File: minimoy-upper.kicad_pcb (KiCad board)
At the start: 2 copper layers, 35 x 35 mm, 29 parts, among them J2 Conn_02x02_Odd_Even, J5 AudioJack3_Ground, J6 Conn_02x02_Odd_Even, J7 AudioJack3_Ground, U1 MAX5440EAG, U3 OPA2134, U4 L7805

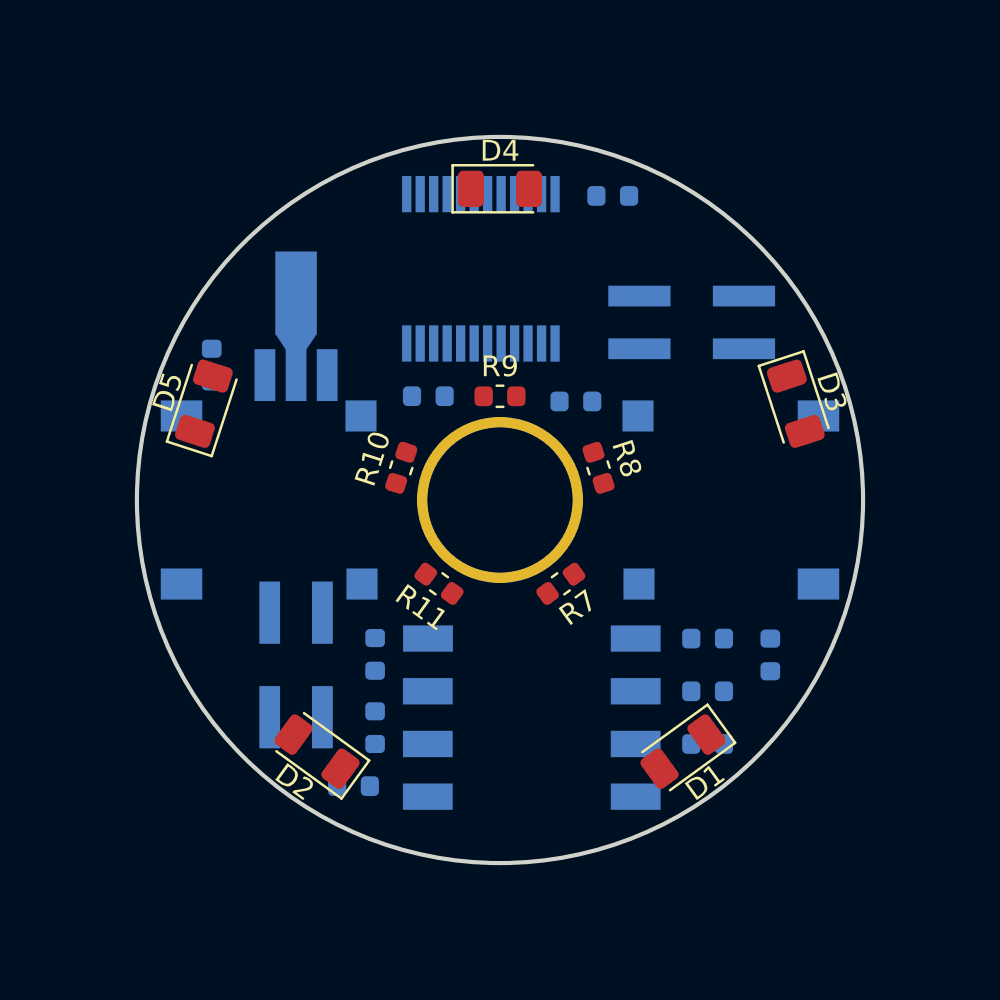
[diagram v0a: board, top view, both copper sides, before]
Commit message: Move 7805 to lower board. Make room for cap on upper board.
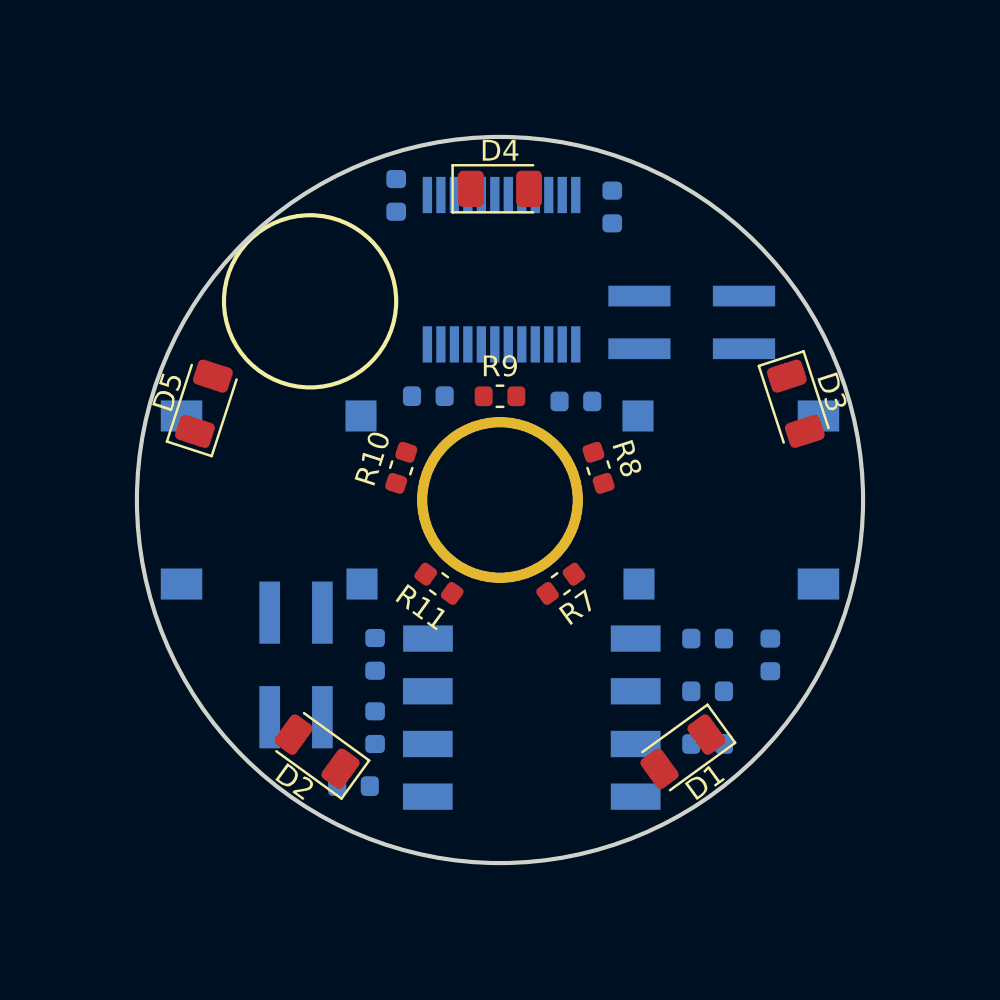
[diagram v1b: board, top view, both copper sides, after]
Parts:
- removed U4: L7805, Package_TO_SOT_SMD:SOT-89-3_Handsoldering
- moved C3 12.1 mm to (95.0, 85.3)
- moved U1 1.00 mm to (100.1, 88.9)
- moved C1 0.53 mm to (105.4, 85.9), turned to 270 degrees
- turned J6 to 270 degrees
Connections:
- J6 pad 2: /VGND_UPPER -> /+5V_UPPER
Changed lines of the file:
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@@
   (general
     (thickness 1.6)
-    (drawings 1)
+    (drawings 2)
     (tracks 0)
     (zones 0)
-    (modules 29)
+    (modules 28)
     (nets 35)
   )
@@
   )
   (module Capacitor_SMD:C_0603_1608Metric (layer B.Cu)
-    (at 105.4355 85.344 180)
+    (at 105.41 85.8775 270)
     (descr "Capacitor SMD 0603 (1608 Metric), square (rectangular) end terminal, IPC_7351 nominal, (Body size source: http://www.tortai-tech.com/upload/download/2011102023233369053.pdf), generated with kicad-footprint-generator")
     (tags capacitor)
     (attr smd)
-    (fp_text reference C1 (at 0 1.43 180) (layer B.SilkS)
-      (effects (font (size 1 1) (thickness 0.15)) (justify mirror))
-    )
-    (fp_text value 0.1uF (at 0 -1.43 180) (layer B.Fab)
+    (fp_text reference C1 (at 0 1.43 270) (layer B.SilkS)
+      (effects (font (size 1 1) (thickness 0.15)) (justify mirror))
+    )
+    (fp_text value 0.1uF (at 0 -1.43 270) (layer B.Fab)
       (effects (font (size 1 1) (thickness 0.15)) (justify mirror))
     )
@@
     (fp_line (start 1.48 0.73) (end 1.48 -0.73) (layer B.CrtYd) (width 0.05))
     (fp_line (start 1.48 -0.73) (end -1.48 -0.73) (layer B.CrtYd) (width 0.05))
-    (fp_text user %R (at 0 0 180) (layer B.Fab)
+    (fp_text user %R (at 0 0 270) (layer B.Fab)
       (effects (font (size 0.4 0.4) (thickness 0.06)) (justify mirror))
     )
-    (pad 1 smd roundrect (at -0.7875 0 180) (size 0.875 0.95) (layers B.Cu B.Paste B.Mask) (roundrect_rratio 0.25)
+    (pad 1 smd roundrect (at -0.7875 0 270) (size 0.875 0.95) (layers B.Cu B.Paste B.Mask) (roundrect_rratio 0.25)
       (net 1 "Net-(C1-Pad1)"))
-    (pad 2 smd roundrect (at 0.7875 0 180) (size 0.875 0.95) (layers B.Cu B.Paste B.Mask) (roundrect_rratio 0.25)
+    (pad 2 smd roundrect (at 0.7875 0 270) (size 0.875 0.95) (layers B.Cu B.Paste B.Mask) (roundrect_rratio 0.25)
       (net 2 /VGND_UPPER))
     (model ${KISYS3DMOD}/Capacitor_SMD.3dshapes/C_0603_1608Metric.wrl
@@
   )
   (module Capacitor_SMD:C_0603_1608Metric (layer B.Cu)
-    (at 86.106 93.4975 270)
+    (at 94.996 85.3185 270)
     (descr "Capacitor SMD 0603 (1608 Metric), square (rectangular) end terminal, IPC_7351 nominal, (Body size source: http://www.tortai-tech.com/upload/download/2011102023233369053.pdf), generated with kicad-footprint-generator")
     (tags capacitor)
@@
   )
   (module Connector_PinSocket_2.54mm:PinSocket_2x02_P2.54mm_Vertical_SMD (layer B.Cu)
-    (at 90.17 107.95 90)
+    (at 90.17 107.95 270)
     (descr "surface-mounted straight socket strip, 2x02, 2.54mm pitch, double cols (from Kicad 4.0.7), script generated")
     (tags "Surface mounted socket strip SMD 2x02 2.54mm double row")
     (attr smd)
-    (fp_text reference J6 (at 0 4.04 90) (layer B.SilkS)
-      (effects (font (size 1 1) (thickness 0.15)) (justify mirror))
-    )
-    (fp_text value Conn_02x02_Odd_Even (at 0 -4.04 90) (layer B.Fab)
-      (effects (font (size 1 1) (thickness 0.15)) (justify mirror))
-    )
-    (fp_text user %R (at 0 0) (layer B.Fab)
+    (fp_text reference J6 (at 0 4.04 270) (layer B.SilkS)
+      (effects (font (size 1 1) (thickness 0.15)) (justify mirror))
+    )
+    (fp_text value Conn_02x02_Odd_Even (at 0 -4.04 270) (layer B.Fab)
+      (effects (font (size 1 1) (thickness 0.15)) (justify mirror))
+    )
+    (fp_text user %R (at 0 0 180) (layer B.Fab)
       (effects (font (size 1 1) (thickness 0.15)) (justify mirror))
     )
@@
     (fp_line (start 2.6 2.6) (end 2.6 2.03) (layer B.SilkS) (width 0.12))
     (fp_line (start -2.6 2.6) (end 2.6 2.6) (layer B.SilkS) (width 0.12))
-    (pad 4 smd rect (at -2.52 -1.27 90) (size 3 1) (layers B.Cu B.Paste B.Mask)
-      (net 2 /VGND_UPPER))
-    (pad 3 smd rect (at 2.52 -1.27 90) (size 3 1) (layers B.Cu B.Paste B.Mask)
+    (pad 4 smd rect (at -2.52 -1.27 270) (size 3 1) (layers B.Cu B.Paste B.Mask)
+      (net 2 /VGND_UPPER))
+    (pad 3 smd rect (at 2.52 -1.27 270) (size 3 1) (layers B.Cu B.Paste B.Mask)
       (net 24 /-12V_UPPER))
-    (pad 2 smd rect (at -2.52 1.27 90) (size 3 1) (layers B.Cu B.Paste B.Mask)
-      (net 2 /VGND_UPPER))
-    (pad 1 smd rect (at 2.52 1.27 90) (size 3 1) (layers B.Cu B.Paste B.Mask)
+    (pad 2 smd rect (at -2.52 1.27 270) (size 3 1) (layers B.Cu B.Paste B.Mask)
+      (net 4 /+5V_UPPER))
+    (pad 1 smd rect (at 2.52 1.27 270) (size 3 1) (layers B.Cu B.Paste B.Mask)
       (net 25 /+12V_UPPER))
     (model ${KISYS3DMOD}/Connector_PinSocket_2.54mm.3dshapes/PinSocket_2x02_P2.54mm_Vertical_SMD.wrl
@@
   )
   (module Package_SO:SSOP-24_5.3x8.2mm_P0.65mm (layer B.Cu)
-    (at 99.079 88.856 270)
+    (at 100.076 88.9 270)
     (descr "24-Lead Plastic Shrink Small Outline (SS)-5.30 mm Body [SSOP] (see Microchip Packaging Specification 00000049BS.pdf)")
     (tags "SSOP 0.65")
@@
       (net 24 /-12V_UPPER))
   )
-  (module Package_TO_SOT_SMD:SOT-89-3_Handsoldering (layer B.Cu)
-    (at 90.17 92 90)
-    (descr "SOT-89-3 Handsoldering")
-    (tags "SOT-89-3 Handsoldering")
-    (attr smd)
-    (fp_text reference U4 (at 0.45 3.3 90) (layer B.SilkS)
-      (effects (font (size 1 1) (thickness 0.15)) (justify mirror))
-    )
-    (fp_text value L7805 (at 0.5 -3.15 90) (layer B.Fab)
-      (effects (font (size 1 1) (thickness 0.15)) (justify mirror))
-    )
-    (fp_text user %R (at 0.38 0) (layer B.Fab)
-      (effects (font (size 0.6 0.6) (thickness 0.09)) (justify mirror))
-    )
-    (fp_line (start -3.5 -2.55) (end 4.25 -2.55) (layer B.CrtYd) (width 0.05))
-    (fp_line (start 4.25 -2.55) (end 4.25 2.55) (layer B.CrtYd) (width 0.05))
-    (fp_line (start 4.25 2.55) (end -3.5 2.55) (layer B.CrtYd) (width 0.05))
-    (fp_line (start -3.5 2.55) (end -3.5 -2.55) (layer B.CrtYd) (width 0.05))
-    (fp_line (start 1.78 -1.2) (end 1.78 -2.4) (layer B.SilkS) (width 0.12))
-    (fp_line (start 1.78 -2.4) (end -0.92 -2.4) (layer B.SilkS) (width 0.12))
-    (fp_line (start -2.22 2.4) (end 1.78 2.4) (layer B.SilkS) (width 0.12))
-    (fp_line (start 1.78 2.4) (end 1.78 1.2) (layer B.SilkS) (width 0.12))
-    (fp_line (start -0.92 1.51) (end -0.13 2.3) (layer B.Fab) (width 0.1))
-    (fp_line (start 1.68 2.3) (end 1.68 -2.3) (layer B.Fab) (width 0.1))
-    (fp_line (start 1.68 -2.3) (end -0.92 -2.3) (layer B.Fab) (width 0.1))
-    (fp_line (start -0.92 -2.3) (end -0.92 1.51) (layer B.Fab) (width 0.1))
-    (fp_line (start -0.13 2.3) (end 1.68 2.3) (layer B.Fab) (width 0.1))
-    (pad 1 smd rect (at -1.98 1.5 180) (size 1 2.5) (layers B.Cu B.Paste B.Mask)
-      (net 25 /+12V_UPPER))
-    (pad 2 smd rect (at -1.98 0 180) (size 1 2.5) (layers B.Cu B.Paste B.Mask)
-      (net 2 /VGND_UPPER))
-    (pad 3 smd rect (at -1.98 -1.5 180) (size 1 2.5) (layers B.Cu B.Paste B.Mask)
-      (net 4 /+5V_UPPER))
-    (pad 2 smd rect (at 1.98 0 180) (size 2 4) (layers B.Cu B.Paste B.Mask)
-      (net 2 /VGND_UPPER))
-    (pad 2 smd trapezoid (at -0.37 0) (size 1.5 0.75) (rect_delta 0 -0.5 ) (layers B.Cu B.Paste B.Mask)
-      (net 2 /VGND_UPPER))
-    (model ${KISYS3DMOD}/Package_TO_SOT_SMD.3dshapes/SOT-89-3.wrl
-      (at (xyz 0 0 0))
-      (scale (xyz 1 1 1))
-      (rotate (xyz 0 0 0))
-    )
-  )
   (module footprints:hole (layer F.Cu)
     (at 100 100)
@@
     (pad "" np_thru_hole circle (at 0 0) (size 8 8) (drill 7) (layers *.Cu *.Mask))
   )
+  (gr_circle (center 90.846 90.424) (end 94.996 90.424) (layer F.SilkS) (width 0.2))
   (gr_circle (center 100 100) (end 117.5 100) (layer Edge.Cuts) (width 0.2))
 )

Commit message: Larger PCB.
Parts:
- moved C5 16.0 mm to (91.7, 110.2)
- moved R1 8.75 mm to (108.3, 117.8), turned to 0 degrees
- moved R4 7.05 mm to (108.3, 112.7), turned to 0 degrees
- moved C1 6.73 mm to (102.6, 79.8), turned to 180 degrees
- moved R3 5.80 mm to (91.7, 112.8), turned to 0 degrees
- moved R5 4.91 mm to (91.7, 115.3), turned to 180 degrees
- moved J5 4.70 mm to (116.2, 100.0)
- moved J7 4.70 mm to (83.8, 100.0)
- moved J6 4.65 mm to (86.0, 110.0), turned to 90 degrees
- moved R2 4.25 mm to (91.7, 117.9), turned to 180 degrees
- moved C7 4.10 mm to (103.1, 91.2)
- moved J2 4.03 mm to (113.0, 90.0), turned to 90 degrees
- moved U3 3.83 mm to (100.0, 114.0)
- moved R6 3.83 mm to (108.3, 115.2)
- moved C6 3.80 mm to (108.4, 110.1)
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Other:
- board size 35 x 35 mm -> 44 x 44 mm
